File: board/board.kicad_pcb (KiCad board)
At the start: 2 copper layers, 21 x 29 mm, 38 parts, among them J1 001_I2C, J2 Conn_01x06_Male, Q1 SSM3K361R, Q2 SSM3K361R, Q3 SSM3K361R, Q4 SSM3K361R, U1 TPS23861

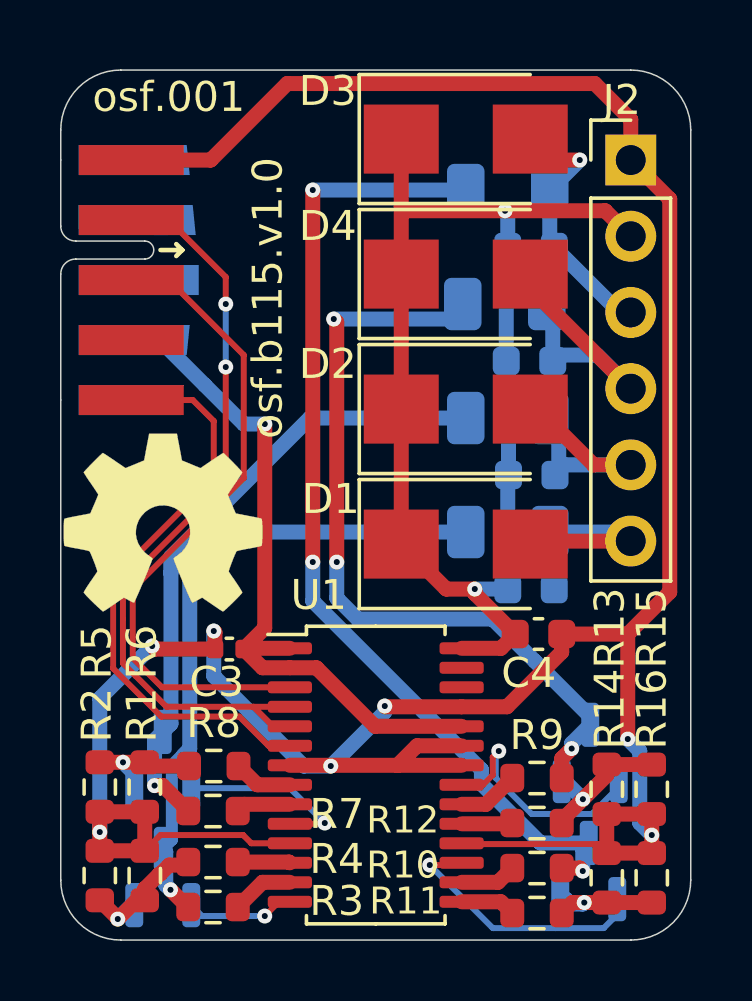
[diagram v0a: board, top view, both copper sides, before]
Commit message: broke out address lines
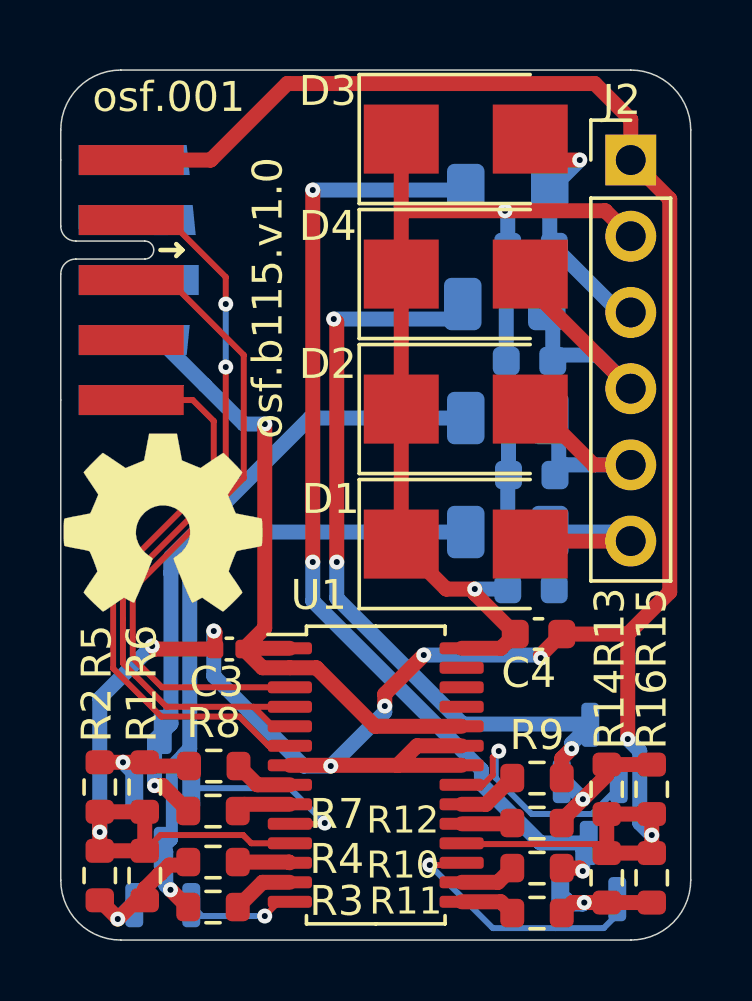
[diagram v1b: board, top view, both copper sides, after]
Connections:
- U1 pad 25: GND -> /poe_pse/AIN
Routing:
- net GND: vias 7 -> 9
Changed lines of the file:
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@@
   (net 34 "/poe_pse/AOUT")
   (net 35 "unconnected-(U1-Pad27)")
+  (net 36 "/poe_pse/AIN")
   (footprint "Diode_SMD:D_SMB" (layer "F.Cu")
     (at 153.5 96.8)
@@
       (net 5 "+3.3V") (pinfunction "SHTDWN") (pintype "input"))
     (pad "25" smd roundrect (at 2.8625 -2.275) (size 1.475 0.4) (layers "F.Cu" "F.Paste" "F.Mask") (roundrect_rratio 0.25)
-      (net 4 "GND") (pinfunction "AIN") (pintype "input"))
+      (net 36 "/poe_pse/AIN") (pinfunction "AIN") (pintype "input"))
     (pad "26" smd roundrect (at 2.8625 -2.925) (size 1.475 0.4) (layers "F.Cu" "F.Paste" "F.Mask") (roundrect_rratio 0.25)
       (net 34 "/poe_pse/AOUT") (pinfunction "AOUT") (pintype "output"))
@@
   (segment (start 158.2 114.8) (end 158.2 116.1) (width 0.5) (layer "F.Cu") (net 4))
   (segment (start 153.3625 113.175) (end 151.225 113.175) (width 0.5) (layer "F.Cu") (net 4))
-  (segment (start 156.7 109.4) (end 154.875 111.225) (width 0.5) (layer "F.Cu") (net 4))
+  (segment (start 150.8 111.2) (end 150.8 110.8) (width 0.5) (layer "F.Cu") (net 4))
   (segment (start 158.2 116.1) (end 159.7 116.1) (width 0.5) (layer "F.Cu") (net 4))
   (segment (start 158.9 108.8) (end 158.9 112.3) (width 0.5) (layer "F.Cu") (net 4))
   (segment (start 146.353869 115.775) (end 146.078869 115.5) (width 0.2) (layer "F.Cu") (net 4))
-  (segment (start 154.875 111.225) (end 153.3625 111.225) (width 0.5) (layer "F.Cu") (net 4))
-  (segment (start 153.3625 111.225) (end 150.825 111.225) (width 0.5) (layer "F.Cu") (net 4))
   (segment (start 141.3 116.025) (end 141.3 115.4) (width 0.5) (layer "F.Cu") (net 4))
   (segment (start 143.325 115.5) (end 142.8 116.025) (width 0.2) (layer "F.Cu") (net 4))
@@
   (segment (start 145.1 108.7) (end 145.14 108.74) (width 0.5) (layer "F.Cu") (net 4))
   (segment (start 141.3 114.725) (end 142.8 114.725) (width 0.5) (layer "F.Cu") (net 4))
+  (segment (start 150.8 110.8) (end 152.1 109.5) (width 0.5) (layer "F.Cu") (net 4))
   (segment (start 158.9 108.8) (end 160.3 107.4) (width 0.5) (layer "F.Cu") (net 4))
-  (segment (start 156.7 108.8) (end 156.7 109.4) (width 0.5) (layer "F.Cu") (net 4))
   (segment (start 151.875 112.525) (end 151.225 113.175) (width 0.5) (layer "F.Cu") (net 4))
   (segment (start 159 93) (end 159 91.65) (width 0.5) (layer "F.Cu") (net 4))
+  (segment (start 156 109.5) (end 156.7 108.8) (width 0.5) (layer "F.Cu") (net 4))
   (segment (start 157.8 90.45) (end 147.55 90.45) (width 0.5) (layer "F.Cu") (net 4))
   (segment (start 147.6375 113.175) (end 148.975 113.175) (width 0.5) (layer "F.Cu") (net 4))
@@
   (segment (start 146.078869 115.5) (end 143.325 115.5) (width 0.2) (layer "F.Cu") (net 4))
   (segment (start 156.7 108.8) (end 158.9 108.8) (width 0.5) (layer "F.Cu") (net 4))
+  (segment (start 156 109.6) (end 156 109.5) (width 0.5) (layer "F.Cu") (net 4))
   (segment (start 143.1465 109.3) (end 143.0465 109.2) (width 0.5) (layer "F.Cu") (net 4))
   (segment (start 153.3625 115.775) (end 153.3895 115.802) (width 0.2) (layer "F.Cu") (net 4))
@@
   (segment (start 147.6375 115.775) (end 146.353869 115.775) (width 0.2) (layer "F.Cu") (net 4))
   (segment (start 145.14 108.74) (end 145.14 109.3) (width 0.5) (layer "F.Cu") (net 4))
-  (segment (start 150.825 111.225) (end 150.8 111.2) (width 0.5) (layer "F.Cu") (net 4))
   (segment (start 157.902 115.802) (end 158.2 116.1) (width 0.2) (layer "F.Cu") (net 4))
   (segment (start 145 93) (end 142.35 93) (width 0.5) (layer "F.Cu") (net 4))
@@
   (segment (start 159.7 115.5) (end 159.7 114.8) (width 0.5) (layer "F.Cu") (net 4))
   (segment (start 147.55 90.45) (end 145 93) (width 0.5) (layer "F.Cu") (net 4))
+  (via (at 152.1 109.5) (size 0.5) (drill 0.2) (layers "F.Cu" "B.Cu") (net 4))
+  (via (at 156 109.6) (size 0.5) (drill 0.2) (layers "F.Cu" "B.Cu") (net 4))
   (via (at 149 113.2) (size 0.5) (drill 0.2) (layers "F.Cu" "B.Cu") (net 4))
   (via (at 145.1 108.7) (size 0.5) (drill 0.2) (layers "F.Cu" "B.Cu") (net 4))
@@
   (segment (start 150.8 111.2) (end 150.8 111.4) (width 0.5) (layer "B.Cu") (net 4))
   (segment (start 143.0465 109.2) (end 141.3 110.9465) (width 0.5) (layer "B.Cu") (net 4))
+  (segment (start 152.1 109.5) (end 155.9 109.5) (width 0.5) (layer "B.Cu") (net 4))
+  (segment (start 155.9 109.5) (end 156 109.6) (width 0.5) (layer "B.Cu") (net 4))
   (segment (start 145.1 108.7) (end 145.1 110.2) (width 0.5) (layer "B.Cu") (net 4))
   (segment (start 145.1 110.2) (end 148.1 113.2) (width 0.5) (layer "B.Cu") (net 4))
@@
   (via (at 149.1 98.3) (size 0.5) (drill 0.2) (layers "F.Cu" "B.Cu") (net 11))
   (via (at 149.2 106.4) (size 0.5) (drill 0.2) (layers "F.Cu" "B.Cu") (net 11))
+  (segment (start 153.4 111.8) (end 149.2 107.6) (width 0.5) (layer "B.Cu") (net 11))
+  (segment (start 157.65 111.825) (end 157.625 111.8) (width 0.5) (layer "B.Cu") (net 11))
   (segment (start 149.2 107.6) (end 149.2 106.4) (width 0.5) (layer "B.Cu") (net 11))
   (segment (start 152.9 98.3) (end 153.4 97.8) (width 0.5) (layer "B.Cu") (net 11))
-  (segment (start 154.4 108.3) (end 149.9 108.3) (width 0.5) (layer "B.Cu") (net 11))
-  (segment (start 149.9 108.3) (end 149.2 107.6) (width 0.5) (layer "B.Cu") (net 11))
+  (segment (start 157.625 111.8) (end 153.4 111.8) (width 0.5) (layer "B.Cu") (net 11))
   (segment (start 149.1 98.3) (end 152.9 98.3) (width 0.5) (layer "B.Cu") (net 11))
-  (segment (start 157.65 111.825) (end 157.65 111.55) (width 0.5) (layer "B.Cu") (net 11))
   (segment (start 157.029928 112.617698) (end 157.029928 112.445072) (width 0.5) (layer "B.Cu") (net 11))
-  (segment (start 157.65 111.55) (end 155.8 109.7) (width 0.5) (layer "B.Cu") (net 11))
   (segment (start 157.029928 112.445072) (end 157.65 111.825) (width 0.5) (layer "B.Cu") (net 11))
-  (segment (start 155.8 109.7) (end 154.4 108.3) (width 0.5) (layer "B.Cu") (net 11))
   (segment (start 147.6375 111.225) (end 146.425 111.225) (width 0.2) (layer "F.Cu") (net 12))
   (segment (start 145.5 103.737552) (end 145.5 99.9) (width 0.2) (layer "F.Cu") (net 12))

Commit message: added lcsc part numbers
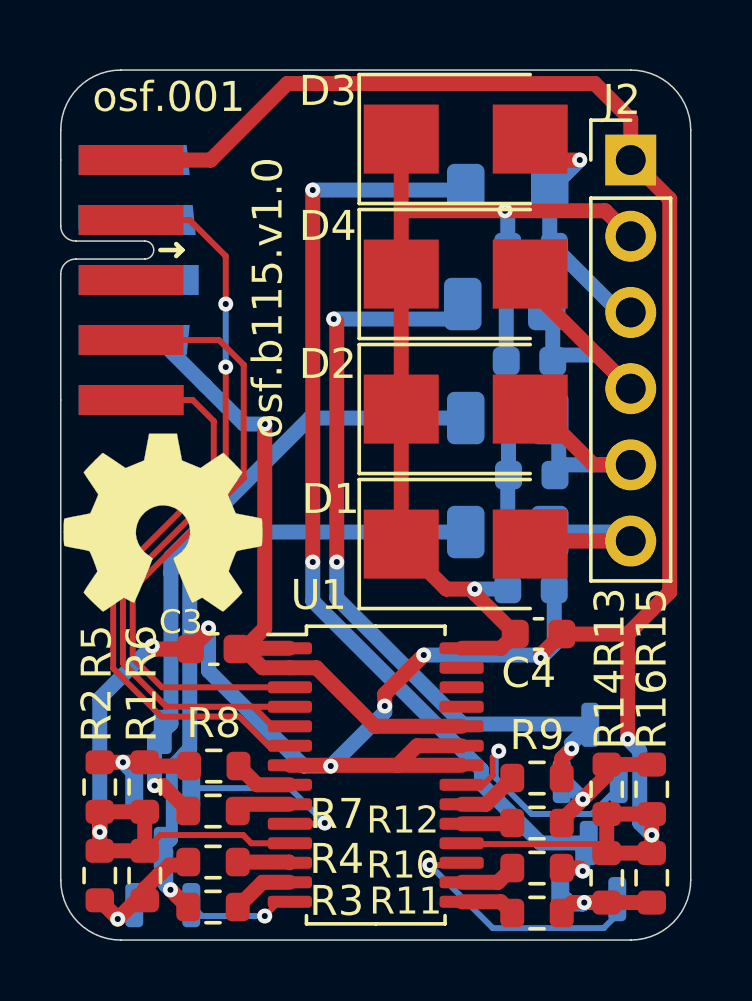
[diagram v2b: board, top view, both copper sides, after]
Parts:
- C3: footprint Capacitor_SMD:C_0402_1005Metric -> Capacitor_SMD:C_0603_1608Metric
- moved C3 0.52 mm to (145.1, 109.3)
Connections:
- C1 pad 2: /poe_pse/switch4 -> GND
- D1 pad 2: /poe_pse/switch4 -> GND
- F1 pad 2: /poe_pse/switch4 -> GND
- J1 pad 3: /poe_pse/SCL -> unconnected-(J1-N/C-Pad3)
- J1 pad 4: unconnected-(J1-Pad4) -> /poe_pse/SCL
- J1 pad 6: (no net) -> unconnected-(J1-CS/EN-Pad6)
- J1 pad 7: (no net) -> unconnected-(J1-status-Pad7)
- J2 pad 6: /poe_pse/switch4 -> GND
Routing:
- net GND: track 101.5 -> 111.9 mm
- net /poe_pse/switch4: track 8.18 -> 0.00 mm
- net /poe_pse/SCL: track 22.1 -> 21.0 mm
